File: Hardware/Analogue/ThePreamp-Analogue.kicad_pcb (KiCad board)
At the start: 2 copper layers, 285 x 65 mm, 45 parts, among them IC1 ULN2803CDWR, J1 To preamp, J10 Switch & trigger outputs and 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, J11 Conn_01x04, J12 Conn_01x03, J13 Conn_01x04, J14 Conn_01x03, J15 Conn_01x02_Pin, J2 From preamp, J3 Digital In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

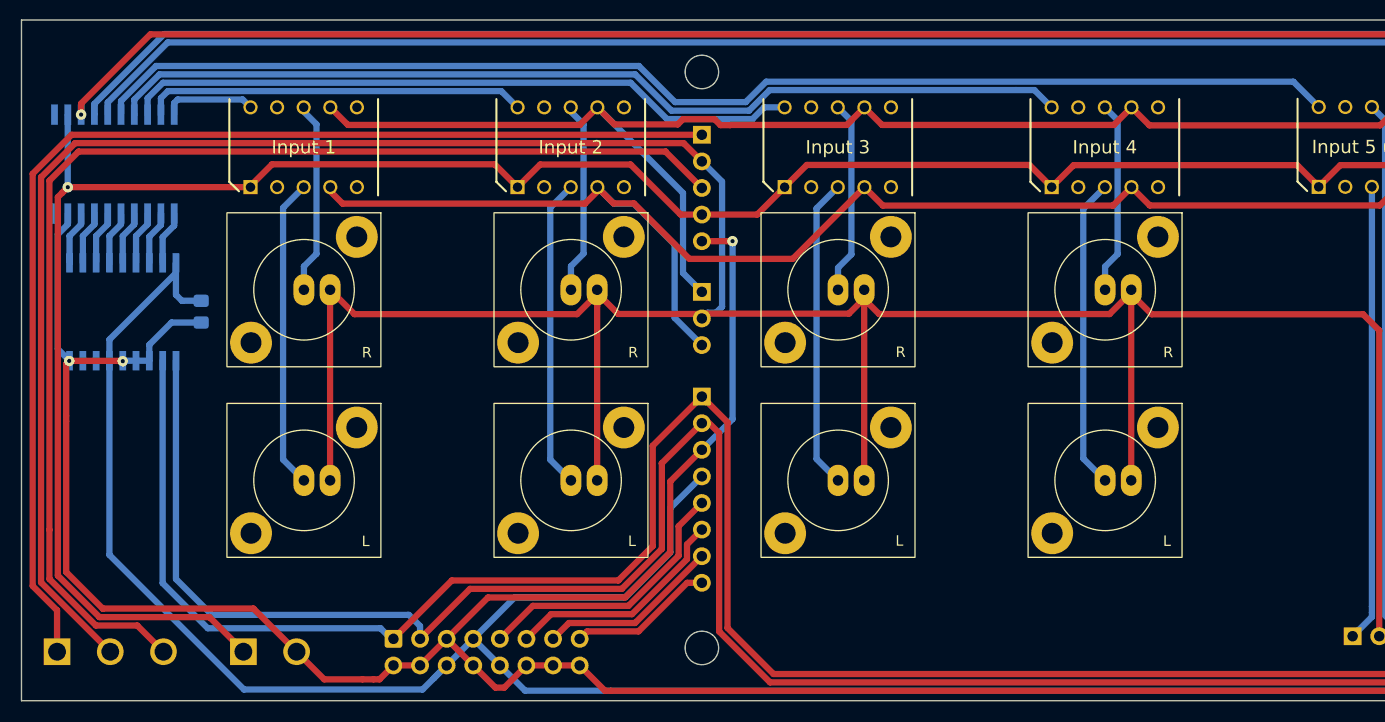
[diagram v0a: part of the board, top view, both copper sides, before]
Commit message: Removed +/-15V connector from analog board
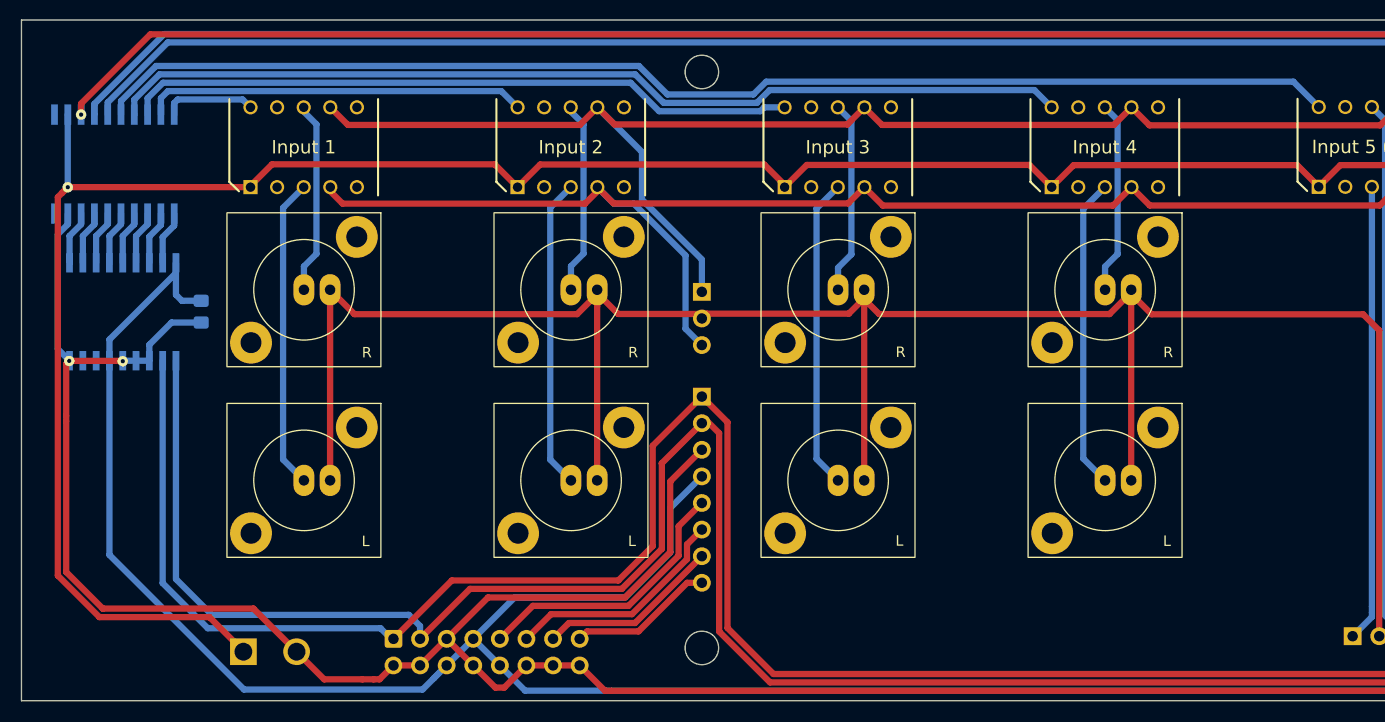
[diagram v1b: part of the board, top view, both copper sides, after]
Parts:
- removed J6: Power Out, Connector_PinSocket_2.54mm:PinSocket_1x05_P2.54mm_Vertical
- removed J7: Audio Power In, THEPREAMP_POWER_CON:TBP01R2-508-03BK (VERT)
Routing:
- net GNDA: track 345.6 -> 215.3 mm
- net -15V: track 116.7 -> 0.00 mm
- net +15V: track 112.0 -> 0.00 mm
- net GND: track 476.9 -> 452.6 mm, vias 3 -> 2
- net Audio L: track 131.9 -> 127.5 mm
- net +12V: track 465.5 -> 463.4 mm
- net RELAY4: track 93.0 -> 92.4 mm
- net RELAY3: track 64.9 -> 64.3 mm
- net RELAY5: track 120.3 -> 119.7 mm

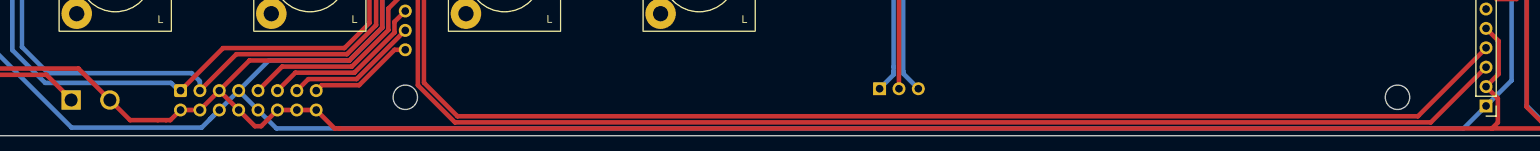
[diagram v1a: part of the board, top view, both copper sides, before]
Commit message: Aligned IDC connector placement between controller and analog pcb
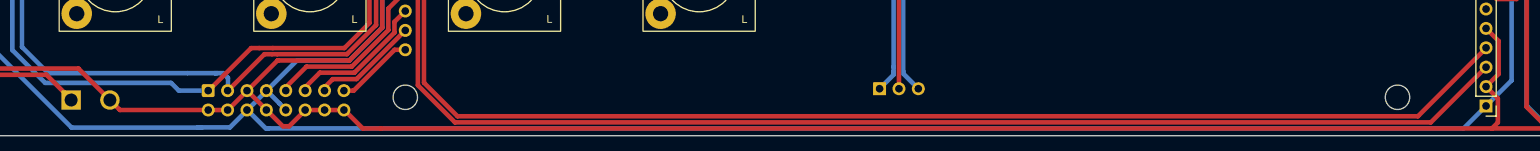
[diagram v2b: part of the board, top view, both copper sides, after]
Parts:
- moved J3 3.63 mm to (48.8, 135.9)
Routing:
- net GND: track 452.6 -> 447.3 mm
- net SPI:MOSI: track 17.5 -> 14.3 mm
- net SPI:MISO: track 21.9 -> 18.7 mm
- net SPI:SS: track 13.9 -> 10.7 mm
- net SPI:SCK: track 26.3 -> 23.1 mm
- net I2C:SDA: track 258.1 -> 257.5 mm
- net I2C:SCL: track 253.3 -> 253.9 mm

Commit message: Pcb dimensions
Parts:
- removed J8: Relay Power In, THEPREAMP_POWER_CON:TBP01R2-508-02BK (VERT)
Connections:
- J3 pad 2: GND -> +12V
- J3 pad 4: GND -> +12V
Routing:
- net +12V: track 463.4 -> 470.6 mm
- net GND: track 447.3 -> 451.1 mm

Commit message: Chassis placement new draft
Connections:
- J3 pad 12: GND -> +12V
- J3 pad 14: GND -> +12V
- J3 pad 16: GND -> +12V
- J3 pad 2: +12V -> GND
- J3 pad 4: +12V -> GND
- J3 pad 8: GND -> +3.3V
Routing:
- net +12V: track 470.6 -> 500.7 mm
- net I2C:SCL: track 253.9 -> 274.3 mm
- net GND: track 451.1 -> 443.1 mm
- net +3.3V: track 302.0 -> 300.0 mm
- net I2C:SDA: track 257.5 -> 256.8 mm
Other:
- board text removed: "+A"
- board text removed: "-A"

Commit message: Moved connector on Analogue pcb
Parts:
- moved J3 33.8 mm to (14.9, 135.8)
- moved G*** 5.77 mm to (230.0, 87.6)
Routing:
- net SPI:SS: track 10.7 -> 44.0 mm
- net SPI:SCK: track 23.1 -> 56.5 mm
- net SPI:MOSI: track 14.3 -> 47.6 mm
- net SPI:MISO: track 18.7 -> 52.1 mm
- net +12V: track 500.7 -> 473.0 mm
- net I2C:SCL: track 274.3 -> 258.6 mm, vias 0 -> 1
- net I2C:SDA: track 256.8 -> 265.4 mm, vias 0 -> 1
- net GND: track 443.1 -> 447.6 mm
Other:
- board text added: "2024-04"
- board text removed: "+12V"
- board text removed: "2024-03"

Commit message: Last changes before ordering of pcb
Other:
- board text added: "12V"
- board text removed: "3.3"
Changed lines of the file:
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@@
 			)
 		)
-		(property "Footprint" ""
+		(property "Footprint" "MountingHole:MountingHole_3.2mm_M3"
 			(at 0 0 0)
 			(unlocked yes)
@@
 			)
 		)
-		(property "Footprint" ""
+		(property "Footprint" "MountingHole:MountingHole_3.2mm_M3"
 			(at 0 0 0)
 			(unlocked yes)
@@
 			)
 		)
-		(property "Footprint" ""
+		(property "Footprint" "MountingHole:MountingHole_3.2mm_M3"
 			(at 0 0 0)
 			(unlocked yes)
@@
 			)
 		)
-		(property "Footprint" ""
+		(property "Footprint" "MountingHole:MountingHole_3.2mm_M3"
 			(at 0 0 0)
 			(unlocked yes)
@@
 			)
 		)
-		(property "Footprint" ""
+		(property "Footprint" "The PreAmp logo:The PreAmp logo"
 			(at 0 0 180)
 			(unlocked yes)
@@
 			)
 		)
-		(property "Footprint" "PinSocket_1x03_P2.54mm_Vertical"
+		(property "Footprint" "Connector_PinSocket_2.54mm:PinSocket_1x03_P2.54mm_Vertical"
 			(at 0 0 0)
 			(unlocked yes)
@@
 			)
 		)
-		(property "Footprint" "PinSocket_1x03_P2.54mm_Vertical"
+		(property "Footprint" "Connector_PinSocket_2.54mm:PinSocket_1x03_P2.54mm_Vertical"
 			(at 0 0 0)
 			(unlocked yes)
@@
 		)
 	)
-	(gr_text "3.3"
+	(gr_text "3V3"
 		(at 20.55 139.44 90)
 		(layer "B.SilkS")
@@
 		)
 	)
+	(gr_text "3V3"
+		(at 23.15 139.43 90)
+		(layer "B.SilkS")
+		(effects
+			(font
+				(size 0.8 0.8)
+				(thickness 0.15)
+			)
+			(justify left bottom mirror)
+		)
+	)
 	(gr_text "Input 5 (Opt.)"
 		(at 144.5 138.9 0)
@@
 		)
 	)
-	(gr_text "3.3"
+	(gr_text "3V3"
 		(at 25.65 139.44 90)
 		(layer "B.SilkS")
@@
 		)
 	)
-	(gr_text "GND"
+	(gr_text "12V"
 		(at 28.13 139.44 90)
 		(layer "B.SilkS")
@@
 	)
 	(gr_text "GND"
-		(at 23.03 139.44 90)
-		(layer "B.SilkS")
-		(effects
-			(font
-				(size 0.8 0.7)
-				(thickness 0.15)
-			)
-			(justify left bottom mirror)
-		)
-	)
-	(gr_text "GND"
 		(at 290.32 101.02 0)
 		(layer "B.SilkS")
@@
 		)
 	)
-	(gr_text "GND"
+	(gr_text "12V"
 		(at 33.24 139.44 90)
 		(layer "B.SilkS")
@@
 		)
 	)
-	(gr_text "GND"
+	(gr_text "12V\n"
 		(at 30.67 139.44 90)
 		(layer "B.SilkS")

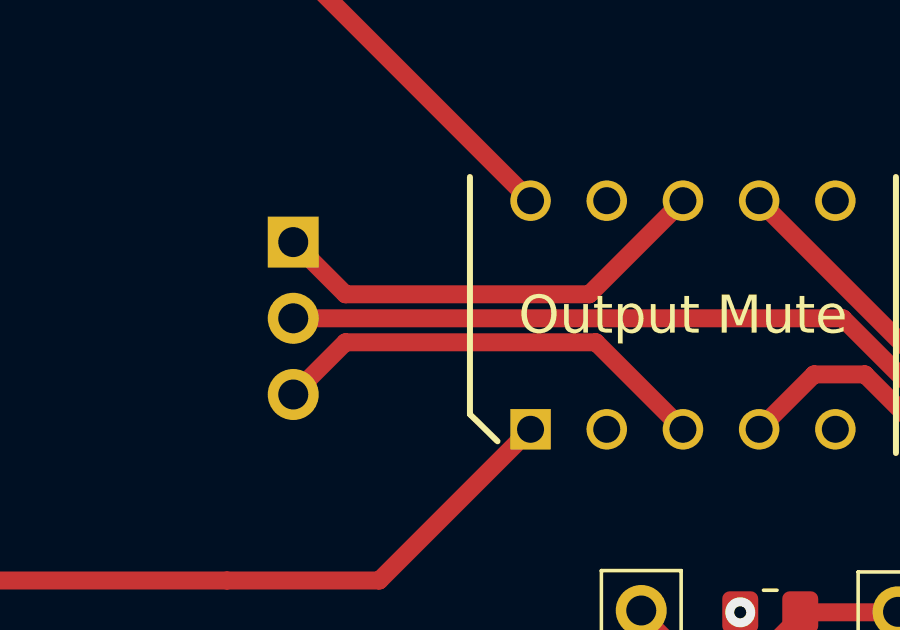
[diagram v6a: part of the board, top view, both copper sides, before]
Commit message: pcb bug output relay fixed - when off output should be shorted to ground a
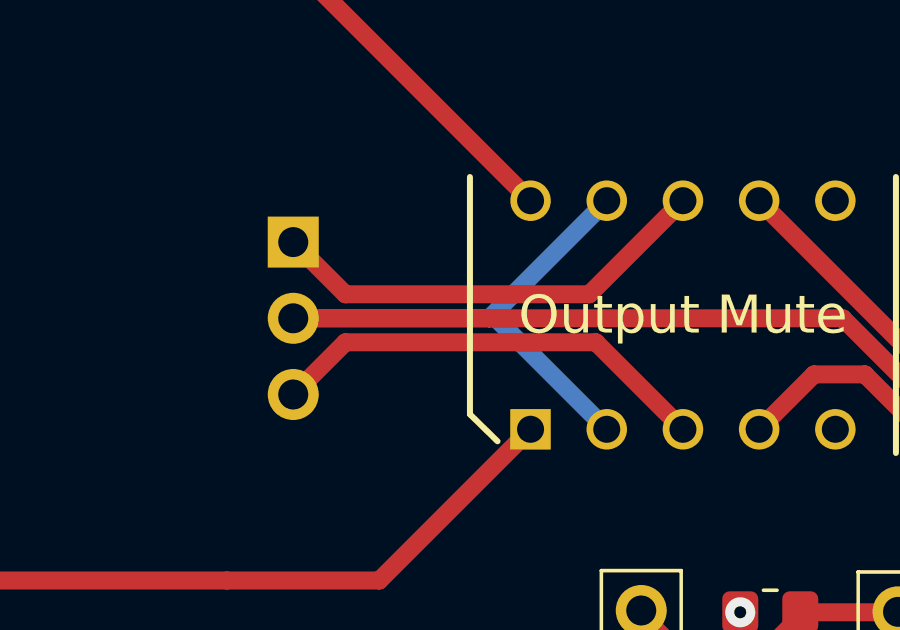
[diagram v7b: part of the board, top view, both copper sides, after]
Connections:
- K6 pad 2: unconnected-(K6-Pad2) -> GNDA_OUT
- K6 pad 9: unconnected-(K6-Pad9) -> GNDA_OUT
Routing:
- net GNDA_OUT: track 66.6 -> 84.1 mm

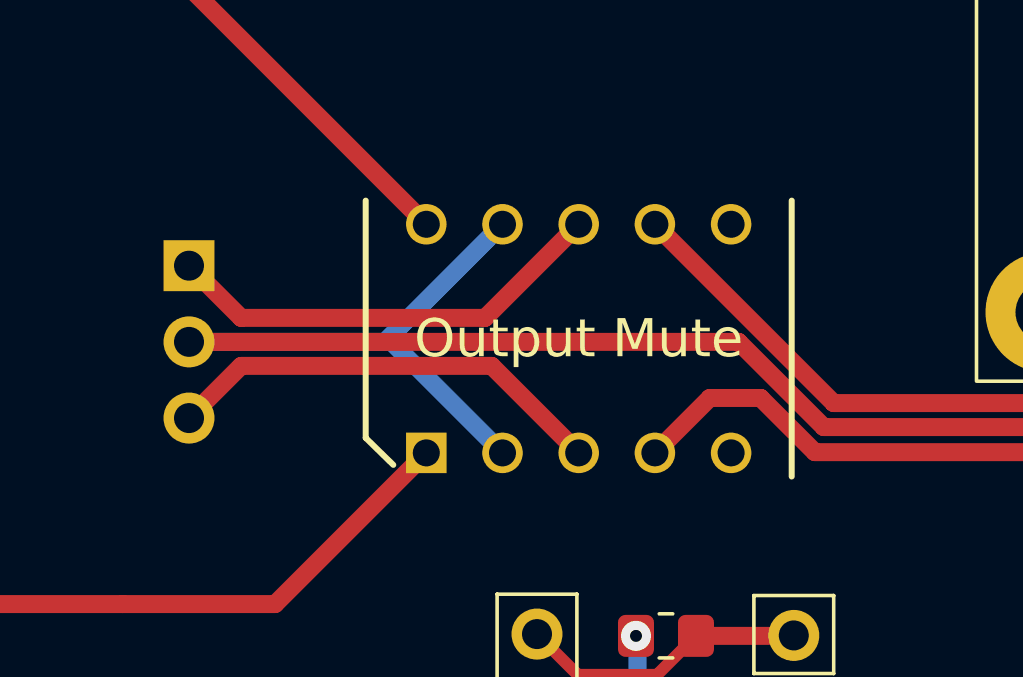
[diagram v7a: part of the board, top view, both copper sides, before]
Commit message: Fixed output relay wiring on analog board schematic & pcb
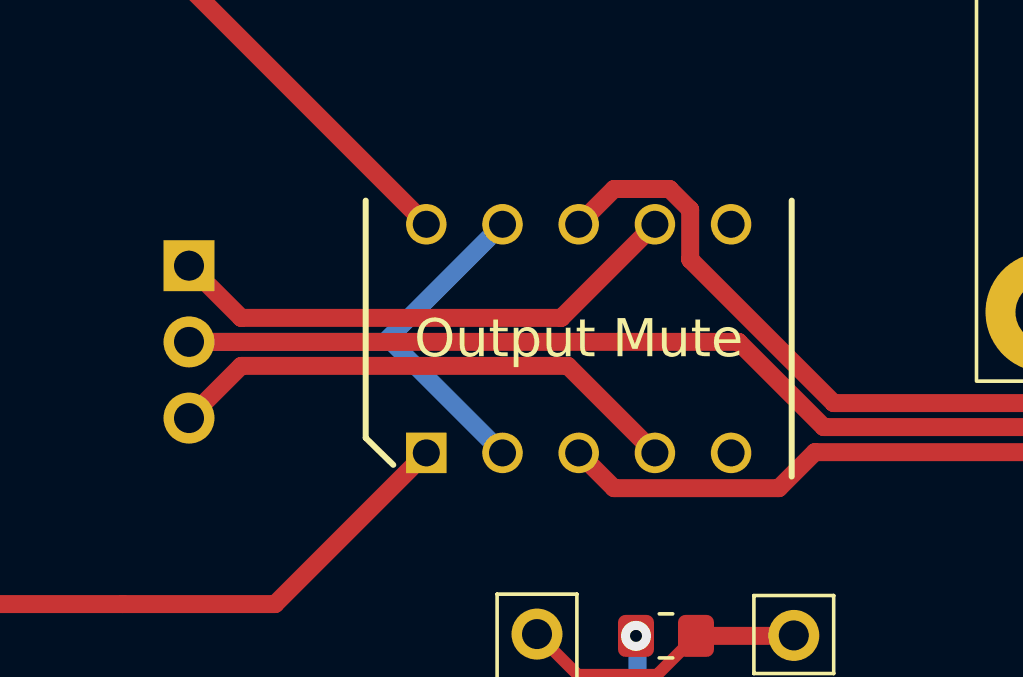
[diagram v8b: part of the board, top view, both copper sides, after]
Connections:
- K6 pad 3: Audio L out -> Net-(RCA5-In)
- K6 pad 4: Net-(RCA5-In) -> Audio L out
- K6 pad 7: Net-(RCA10-In) -> Audio R out
- K6 pad 8: Audio R out -> Net-(RCA10-In)
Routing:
- net Net-(RCA10-In): track 27.5 -> 32.0 mm
- net Audio R out: track 15.1 -> 17.7 mm
- net Audio L out: track 15.0 -> 17.6 mm
- net Net-(RCA5-In): track 38.7 -> 40.8 mm
